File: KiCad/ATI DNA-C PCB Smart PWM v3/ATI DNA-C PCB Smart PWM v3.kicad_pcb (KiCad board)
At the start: 2 copper layers, 70 x 20 mm, 17 parts, among them U1 SmartPWMv3

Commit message: Make pretty
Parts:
- added REF**: 0.36_inch_VM, ATI DNA-C PCB Smart PWM v3:0.36_inch_VM, F.Cu at (141.7, 100.3)
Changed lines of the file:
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@@
     (tracks 81)
     (zones 0)
-    (modules 17)
+    (modules 18)
     (nets 16)
   )
@@
     (add_net "Net-(U1-Pad9)")
   )
+  (module "ATI DNA-C PCB Smart PWM v3:0.36_inch_VM" (layer F.Cu)
+    (at 141.72 100.27)
+    (fp_text reference REF** (at 0 -2.69) (layer F.SilkS)
+      (effects (font (size 1 1) (thickness 0.15)))
+    )
+    (fp_text value 0.36_inch_VM (at 0 -0.73) (layer F.Fab) hide
+      (effects (font (size 1 1) (thickness 0.15)))
+    )
+    (fp_line (start 11.2781 -7.3084) (end -11.5219 -7.3084) (layer F.SilkS) (width 0.15))
+    (fp_line (start -11.5219 -7.3084) (end -11.5219 6.9516) (layer F.SilkS) (width 0.15))
+    (fp_line (start -11.5219 6.9516) (end 11.2781 6.9516) (layer F.SilkS) (width 0.15))
+    (fp_line (start 11.2781 6.9516) (end 11.2781 -7.3084) (layer F.SilkS) (width 0.15))
+    (model "${KIPRJMOD}/ATI DNA-C PCB Smart PWM v3.pretty/XDxx09x3.step"
+      (offset (xyz -0.1 0.15 4.45))
+      (scale (xyz 1.018 1 1.022))
+      (rotate (xyz -90 0 0))
+    )
+  )
   (module "ATI DNA-C PCB Smart PWM v3:PAD_24G" (layer F.Cu)

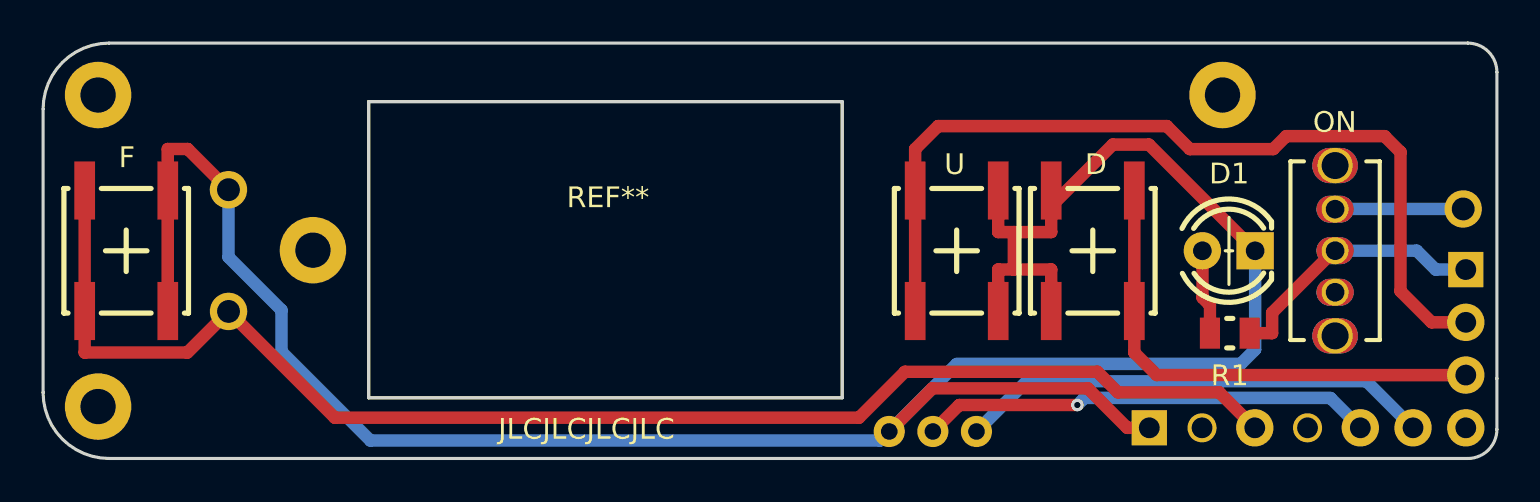
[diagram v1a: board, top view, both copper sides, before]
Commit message: Change/Cleanup 3D models - Add silkscreen gfx
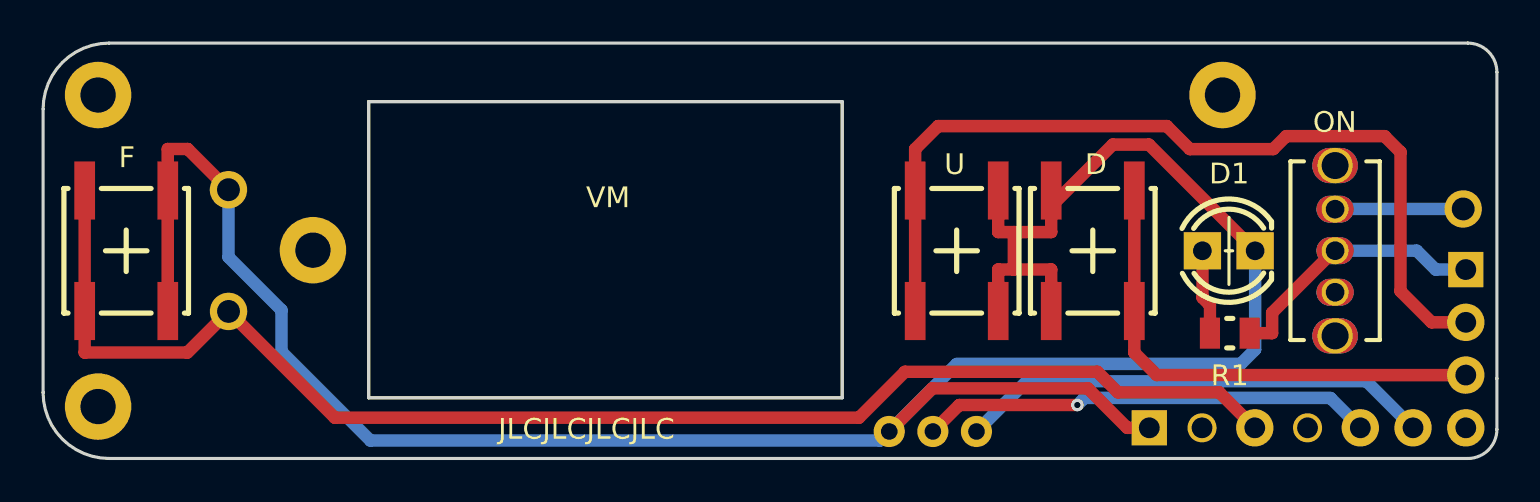
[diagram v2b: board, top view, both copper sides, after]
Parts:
- renumbered REF** to VM
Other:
- board text added: "Designed by MosMax"
- board text added: "Powered by"
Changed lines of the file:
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@@
-(kicad_pcb (version 20171130) (host pcbnew 5.1.0-unknown-7e34a5a~82~ubuntu18.04.1)
+(kicad_pcb (version 20171130) (host pcbnew 5.1.0-unknown-ff73f69~82~ubuntu18.04.1)
   (general
     (thickness 1.6)
-    (drawings 32)
+    (drawings 38)
     (tracks 81)
     (zones 0)
@@
   (page A4)
   (layers
-    (0 F.Cu signal)
-    (31 B.Cu signal)
+    (0 F.Cu signal hide)
+    (31 B.Cu signal hide)
     (32 B.Adhes user)
     (33 F.Adhes user)
     (34 B.Paste user)
-    (35 F.Paste user)
+    (35 F.Paste user hide)
     (36 B.SilkS user)
-    (37 F.SilkS user)
+    (37 F.SilkS user hide)
     (38 B.Mask user)
-    (39 F.Mask user)
+    (39 F.Mask user hide)
     (40 Dwgs.User user hide)
     (41 Cmts.User user)
@@
   (module "ATI DNA-C PCB Smart PWM v3:0.36_inch_VM" (layer F.Cu)
     (at 141.72 100.27)
-    (fp_text reference REF** (at 0 -2.69) (layer F.SilkS)
+    (fp_text reference VM (at 0 -2.69) (layer F.SilkS)
       (effects (font (size 1 1) (thickness 0.15)))
     )
@@
       (rotate (xyz 0 -180 -90))
     )
-    (model /home/madc0w/Desktop/SmartPWMv3/SmartPWMv3/SmartPWMv3.step
-      (offset (xyz -151 92 -6))
+    (model "${KIPRJMOD}/ATI DNA-C PCB Smart PWM v3.pretty/SmartPWM_v3.step"
+      (offset (xyz -15.8 5.2 -5.9))
       (scale (xyz 1 1 1))
       (rotate (xyz 0 0 0))
@@
     (fp_arc (start 0.01 0) (end -2.05 -1.388749) (angle 120.1) (layer F.SilkS) (width 0.25))
     (fp_arc (start 0.01 0.01) (end -1.99 -1.31665) (angle 292.9) (layer F.Fab) (width 0.1))
-    (pad 2 thru_hole circle (at 1.28 0 180) (size 1.8 1.8) (drill 0.9) (layers *.Cu *.Mask)
+    (pad 2 thru_hole rect (at 1.28 0 180) (size 1.8 1.8) (drill 0.9) (layers *.Cu *.Mask)
       (net 12 /LED+))
     (pad 1 thru_hole rect (at -1.26 0 180) (size 1.8 1.8) (drill 0.9) (layers *.Cu *.Mask)
       (net 8 /GND))
-    (model ${KISYS3DMOD}/LED_THT.3dshapes/LED_D4.0mm.wrl
-      (offset (xyz -1.3 0 -1.8))
-      (scale (xyz 1 1 1))
-      (rotate (xyz 0 0 0))
-    )
     (model "${KIPRJMOD}/ATI DNA-C PCB Smart PWM v3.pretty/ELM 2.igs"
       (at (xyz 0 0 0))
       (scale (xyz 1 0.1 1))
       (rotate (xyz -90 0 90))
+    )
+    (model "${KIPRJMOD}/ATI DNA-C PCB Smart PWM v3.pretty/SSL-LX40FT3ID-v0.step"
+      (offset (xyz 0 0 1.3))
+      (scale (xyz 1 1 1))
+      (rotate (xyz 0 0 180))
     )
   )
@@
     (pad 4 smd rect (at 2.9 2 270) (size 2.8 1) (layers F.Cu F.Paste F.Mask)
       (net 1 /Fire) (solder_paste_margin -0.1016) (zone_connect 2))
-    (model "${KIPRJMOD}/ATI DNA-C PCB Smart PWM v3.pretty/430481035816 (rev1).stp"
+    (model "${KIPRJMOD}/ATI DNA-C PCB Smart PWM v3.pretty/omron-tact-color.step"
       (at (xyz 0 0 0))
       (scale (xyz 1 1 1))
-      (rotate (xyz 0 0 0))
+      (rotate (xyz -90 0 0))
     )
   )
@@
     (pad 4 smd rect (at 2.9 2 270) (size 2.8 1) (layers F.Cu F.Paste F.Mask)
       (net 2 /Up) (solder_paste_margin -0.1016) (zone_connect 2))
-    (model "${KIPRJMOD}/ATI DNA-C PCB Smart PWM v3.pretty/430481035816 (rev1).stp"
+    (model "${KIPRJMOD}/ATI DNA-C PCB Smart PWM v3.pretty/omron-tact-color.step"
       (at (xyz 0 0 0))
       (scale (xyz 1 1 1))
-      (rotate (xyz 0 0 0))
+      (rotate (xyz -90 0 0))
     )
   )
@@
     (pad 4 smd rect (at 2.9 2 90) (size 2.8 1) (layers F.Cu F.Paste F.Mask)
       (net 3 /Down) (solder_paste_margin -0.1016) (zone_connect 2))
-    (model "${KIPRJMOD}/ATI DNA-C PCB Smart PWM v3.pretty/430481035816 (rev1).stp"
+    (model "${KIPRJMOD}/ATI DNA-C PCB Smart PWM v3.pretty/omron-tact-color.step"
       (at (xyz 0 0 0))
       (scale (xyz 1 1 1))
-      (rotate (xyz 0 0 0))
-    )
-  )
+      (rotate (xyz -90 0 0))
+    )
+  )
+  (gr_text "Designed by MosMax" (at 161.69 95.29) (layer B.SilkS)
+    (effects (font (size 1 1) (thickness 0.15)) (justify mirror))
+  )
+  (gr_text "Powered by" (at 163.95 97.99) (layer B.SilkS)
+    (effects (font (size 1 1) (thickness 0.15)) (justify mirror))
+  )
+  (gr_poly (pts (xy 156.694106 97.747276) (xy 156.913181 97.743307) (xy 156.360731 96.847163) (xy 156.357556 96.843988) (xy 156.235319 96.647138) (xy 156.210712 96.647138) (xy 155.713031 96.647138) (xy 155.683662 96.647138) (xy 155.458237 96.647138) (xy 155.601113 96.853513) (xy 155.6027 96.853513) (xy 155.867812 97.2742) (xy 155.871781 97.278169) (xy 155.990843 97.469463) (xy 156.043231 97.469463) (xy 156.417087 97.47105) (xy 156.278181 97.282138) (xy 156.101968 97.282138) (xy 156.101175 97.278963) (xy 156.098 97.274994) (xy 155.83765 96.853513) (xy 156.128162 96.853513) (xy 156.694106 97.747276)) (layer B.SilkS) (width 0.007937))
+  (gr_poly (pts (xy 157.214806 98.250513) (xy 156.966363 98.250513) (xy 157.358475 98.952188) (xy 158.558625 96.889232) (xy 158.844375 96.894788) (xy 158.6634 97.218638) (xy 158.459406 97.218638) (xy 158.3205 97.472638) (xy 158.765 97.472638) (xy 159.245219 96.647138) (xy 158.425275 96.647138) (xy 157.352918 98.495782) (xy 157.214806 98.250513)) (layer B.SilkS) (width 0.007937))
+  (gr_poly (pts (xy 157.610887 97.869513) (xy 156.163087 97.869513) (xy 157.364824 99.924532) (xy 158.540368 97.869513) (xy 158.063325 97.869513) (xy 157.931562 98.107638) (xy 158.142699 98.107638) (xy 157.356887 99.410181) (xy 156.595681 98.123513) (xy 157.452931 98.123513) (xy 157.610887 97.869513)) (layer B.SilkS) (width 0.007937))
+  (gr_poly (pts (xy 231.602906 132.562071) (xy 252.928315 132.562071) (xy 252.928315 129.334166) (xy 252.92382 129.153478) (xy 252.910338 128.978526) (xy 252.887874 128.809311) (xy 252.856433 128.645832) (xy 252.81602 128.488089) (xy 252.766639 128.336082) (xy 252.708296 128.189811) (xy 252.640995 128.049277) (xy 252.564741 127.914479) (xy 252.479539 127.785417) (xy 252.385393 127.662091) (xy 252.282309 127.544501) (xy 252.170292 127.432648) (xy 252.049346 127.326531) (xy 251.919475 127.226149) (xy 251.780686 127.131504) (xy 251.632983 127.042595) (xy 251.47637 126.959423) (xy 251.310853 126.881986) (xy 251.136436 126.810285) (xy 250.953124 126.744321) (xy 250.760922 126.684093) (xy 250.559834 126.6296) (xy 250.349867 126.580844) (xy 250.131024 126.537824) (xy 249.90331 126.50054) (xy 249.66673 126.468992) (xy 249.42129 126.443179) (xy 249.166993 126.423103) (xy 248.903845 126.408763) (xy 248.63185 126.400159) (xy 248.351014 126.397291) (xy 237.688294 126.397291) (xy 236.952842 126.409687) (xy 236.264556 126.446849) (xy 235.623478 126.508738) (xy 235.029644 126.595316) (xy 234.483095 126.706543) (xy 233.983868 126.842381) (xy 233.532003 127.002791) (xy 233.127538 127.187735) (xy 232.770511 127.397173) (xy 232.460963 127.631067) (xy 232.324005 127.757173) (xy 232.198931 127.889379) (xy 232.085746 128.027679) (xy 231.984455 128.172068) (xy 231.895062 128.322543) (xy 231.817572 128.479098) (xy 231.75199 128.641728) (xy 231.698322 128.810428) (xy 231.656571 128.985194) (xy 231.626744 129.16602) (xy 231.608843 129.352902) (xy 231.602876 129.545836) (xy 231.602876 132.562071) (xy 231.602906 132.562071)) (layer F.Fab) (width 0.264583))
   (dimension 65.99954 (width 0.12) (layer F.Fab)
     (gr_text "66.000 mm" (at 151.527722 132.664093 -0.2) (layer F.Fab)
